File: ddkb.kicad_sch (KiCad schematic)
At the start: 29 parts, among them J1 Conn_01x04, J2 Conn_01x02, J3 Conn_01x03, SW1 SW_Push, U1 RP2040, U2 NCP1117-3.3_SOT223, U3 W25Q128JVS, Y1 YSX321SL

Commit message: indrease jst marigin
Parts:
- removed J2: Conn_01x02, Button_Switch_SMD:SW_SPST_CK_RS282G05A3, symbol Connector_Generic:Conn_01x02
- added SW2: SW_Push, Button_Switch_SMD:SW_SPST_TL3342, symbol Switch:SW_Push
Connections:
- net GND: now also SW2.1
- net ~{USB_BOOT}: now also SW2.2
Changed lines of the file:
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@@
+    (stroke (width 0) (type default))
+  )
+  (wire (pts (xy 177.8 53.34) (xy 177.8 48.26))
     (stroke (width 0) (type default))
   )
@@
     (stroke (width 0) (type default))
   )
-  (wire (pts (xy 189.23 50.8) (xy 191.008 50.8))
-    (stroke (width 0) (type default))
-  )
   (wire (pts (xy 175.26 99.06) (xy 182.88 99.06))
     (stroke (width 0) (type default))
@@
     (stroke (width 0) (type default))
   )
+  (wire (pts (xy 177.8 48.26) (xy 179.07 48.26))
+    (stroke (width 0) (type default))
+  )
   (wire (pts (xy 255.27 127) (xy 264.16 127))
     (stroke (width 0) (type default))
@@
   )
   (wire (pts (xy 41.91 148.59) (xy 41.91 149.86))
-    (stroke (width 0) (type default))
-  )
-  (wire (pts (xy 191.008 50.8) (xy 191.008 52.832))
     (stroke (width 0) (type default))
   )
@@
     )
   )
-  (symbol (lib_id "power:GND") (at 191.008 52.832 0) (unit 1)
-    (in_bom yes) (on_board yes) (dnp no)
-    (property "Reference" "#PWR08" (at 191.008 59.182 0)
-      (effects (font (size 1.27 1.27)) hide)
-    )
-    (property "Value" "GND" (at 194.564 54.864 0)
-      (effects (font (size 1.27 1.27)))
-    )
-    (property "Footprint" "" (at 191.008 52.832 0)
-      (effects (font (size 1.27 1.27)) hide)
-    )
-    (property "Datasheet" "" (at 191.008 52.832 0)
+  (symbol (lib_id "power:GND") (at 177.8 53.34 0) (unit 1)
+    (in_bom yes) (on_board yes) (dnp no)
+    (property "Reference" "#PWR08" (at 177.8 59.69 0)
+      (effects (font (size 1.27 1.27)) hide)
+    )
+    (property "Value" "GND" (at 181.356 55.372 0)
+      (effects (font (size 1.27 1.27)))
+    )
+    (property "Footprint" "" (at 177.8 53.34 0)
+      (effects (font (size 1.27 1.27)) hide)
+    )
+    (property "Datasheet" "" (at 177.8 53.34 0)
       (effects (font (size 1.27 1.27)) hide)
     )
@@
     )
   )
+  (symbol (lib_id "Switch:SW_Push") (at 184.15 48.26 0) (unit 1)
+    (in_bom yes) (on_board yes) (dnp no) (fields_autoplaced)
+    (property "Reference" "SW2" (at 184.15 41.91 0)
+      (effects (font (size 1.27 1.27)))
+    )
+    (property "Value" "SW_Push" (at 184.15 44.45 0)
+      (effects (font (size 1.27 1.27)))
+    )
+    (property "Footprint" "Button_Switch_SMD:SW_SPST_TL3342" (at 184.15 43.18 0)
+      (effects (font (size 1.27 1.27)) hide)
+    )
+    (property "Datasheet" "~" (at 184.15 43.18 0)
+      (effects (font (size 1.27 1.27)) hide)
+    )
+    (pin "1")
+    (pin "2")
+    (instances
+      (project "ddkb"
+        (path "/85b84858-1c91-402e-8b7c-9a730586bc37"
+          (reference "SW2") (unit 1)
+        )
+      )
+    )
+  )
   (symbol (lib_id "Device:C") (at 80.772 41.91 0) (unit 1)
     (in_bom yes) (on_board yes) (dnp no) (fields_autoplaced)
@@
         )
       )
-    )
-  )
-  (symbol (lib_id "Connector_Generic:Conn_01x02") (at 184.15 48.26 0) (mirror y) (unit 1)
-    (in_bom yes) (on_board yes) (dnp no) (fields_autoplaced)
-    (property "Reference" "J2" (at 184.15 41.91 0)
-      (effects (font (size 1.27 1.27)))
-    )
-    (property "Value" "Conn_01x02" (at 184.15 44.45 0)
-      (effects (font (size 1.27 1.27)))
-    )
-    (property "Footprint" "Button_Switch_SMD:SW_SPST_CK_RS282G05A3" (at 184.15 48.26 0)
-      (effects (font (size 1.27 1.27)) hide)
-    )
-    (property "Datasheet" "~" (at 184.15 48.26 0)
-      (effects (font (size 1.27 1.27)) hide)
-    )
-    (pin "1")
-    (pin "2")
-    (instances
-      (project "ddkb"
-        (path "/85b84858-1c91-402e-8b7c-9a730586bc37"
-          (reference "J2") (unit 1)
-        )
-      )

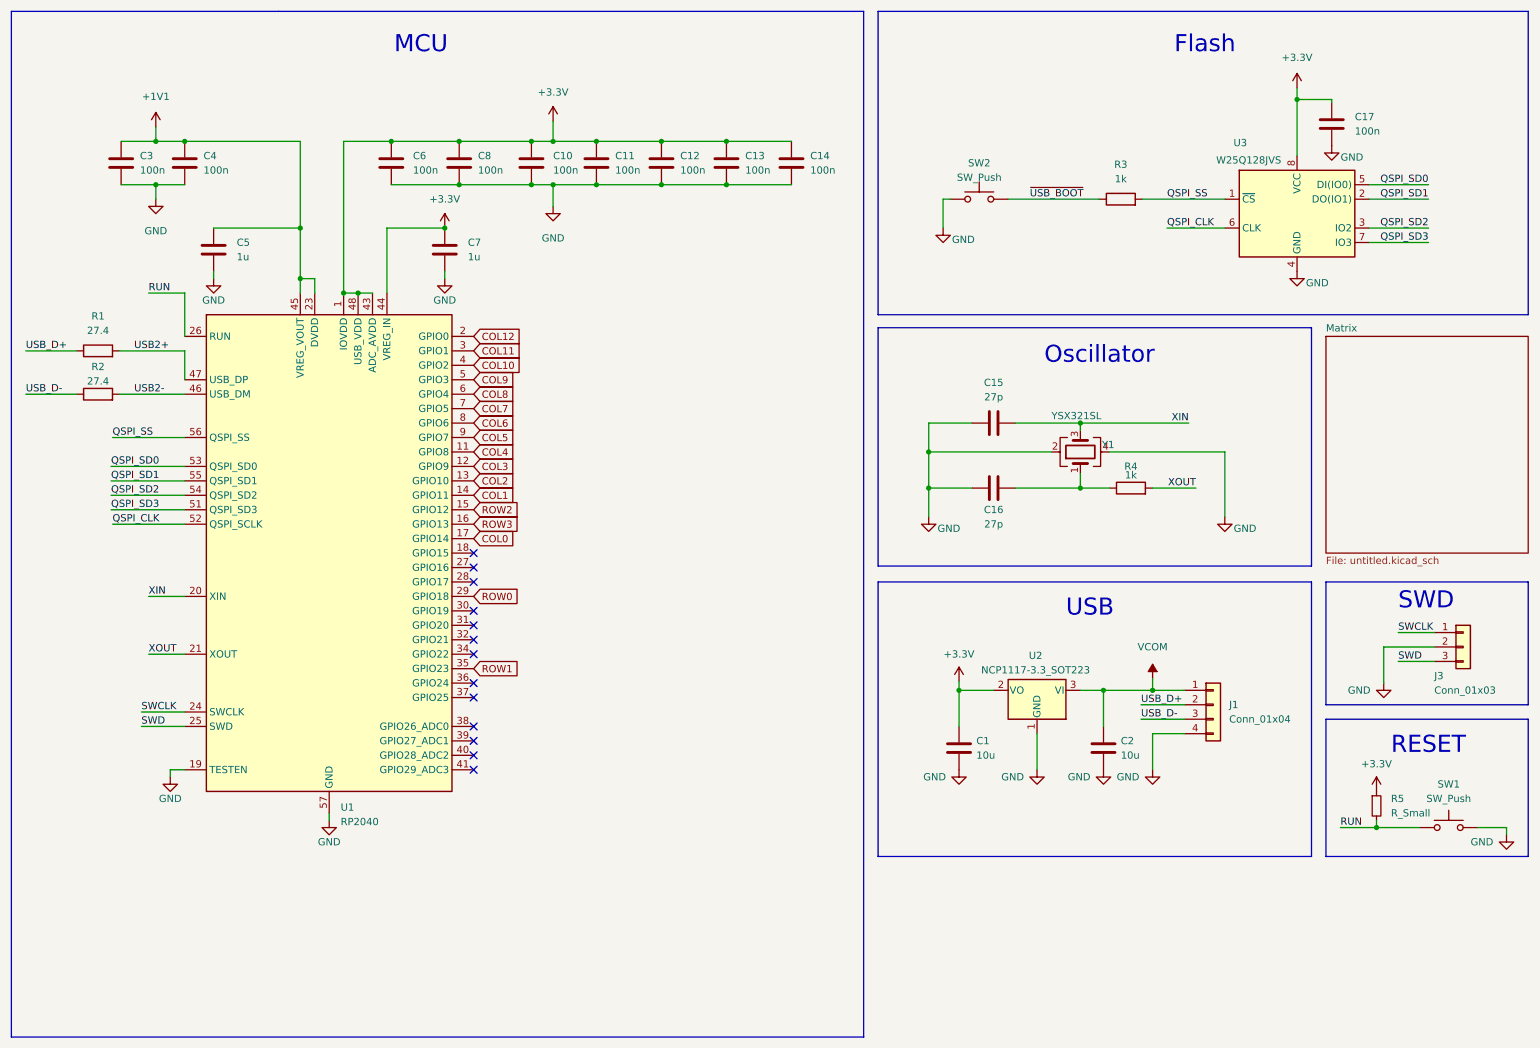
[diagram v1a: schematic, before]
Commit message: add qspi_ss pullup
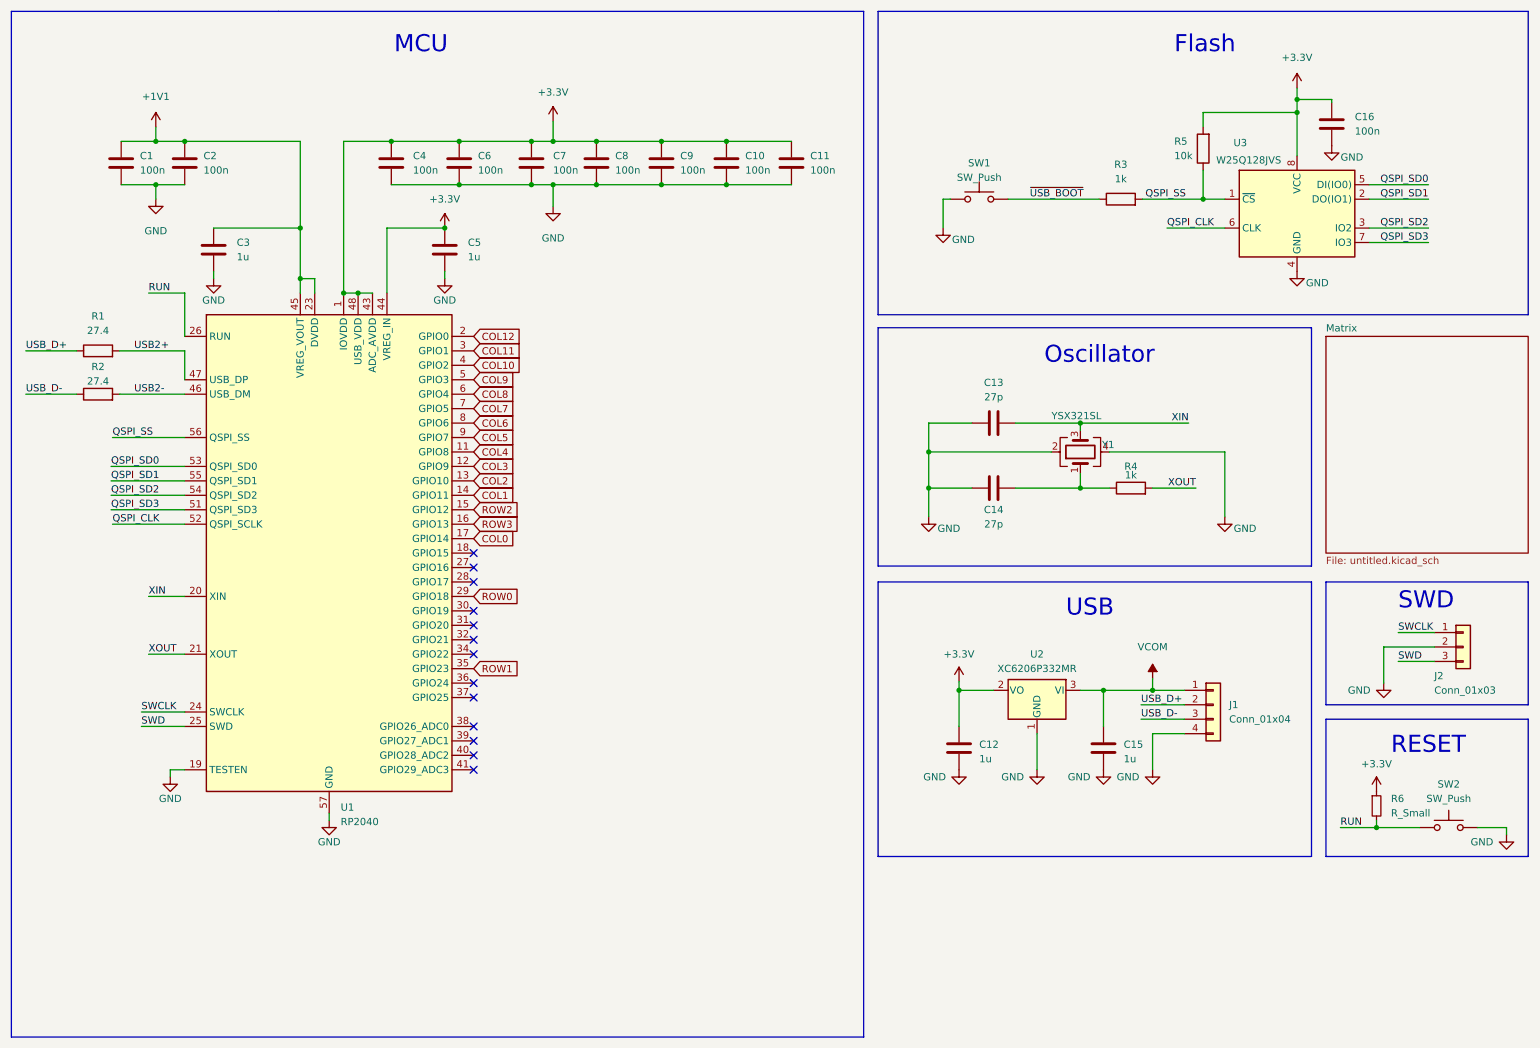
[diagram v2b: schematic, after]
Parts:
- removed U2: NCP1117-3.3_SOT223, Package_TO_SOT_SMD:SOT-223-3_TabPin2, symbol Regulator_Linear:NCP1117-3.3_SOT223
- added R5: 10k, Resistor_SMD:R_0402_1005Metric, symbol Device:R
- added U2: XC6206P332MR, Package_TO_SOT_SMD:SOT-23-3, symbol Regulator_Linear:XC6206PxxxMR
- C12: renamed from C1; value 10u -> 1u
- C15: renamed from C2; value 10u -> 1u
- renumbered C3 to C1, C13 to C10, C14 to C11, C15 to C13, C16 to C14, C17 to C16, C4 to C2, C5 to C3, C6 to C4, C7 to C5, C8 to C6, C10 to C7, C11 to C8, C12 to C9, J3 to J2, R5 to R6, SW2 to SW1, SW1 to SW2
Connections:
- net +3.3V: now also R5.2, U2.2 (VO)
- net GND: now also U2.1 (GND)
- net QSPI_SS: now also R5.1
- net VCOM: now also U2.3 (VI)
